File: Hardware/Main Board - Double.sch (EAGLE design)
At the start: 77 parts, among them J1 MICROMOD-2222-C, J10 MICRO-SD-PUSH-PUSH-EXT-PIN, J2 Vertical Qwiic Connector, J4 QWIIC_RIGHT_ANGLE, J5 CORTEX_JTAG_DEBUG_MINIMUM_PTH, J6 MICROMOD_FUNCTION_MAIN, J7 MICROMOD_FUNCTION_MAIN, Q1 3.1A/30V/105mΩ, U1 STG3856QTR, U2 MCP73831, U5 AP7361C-33

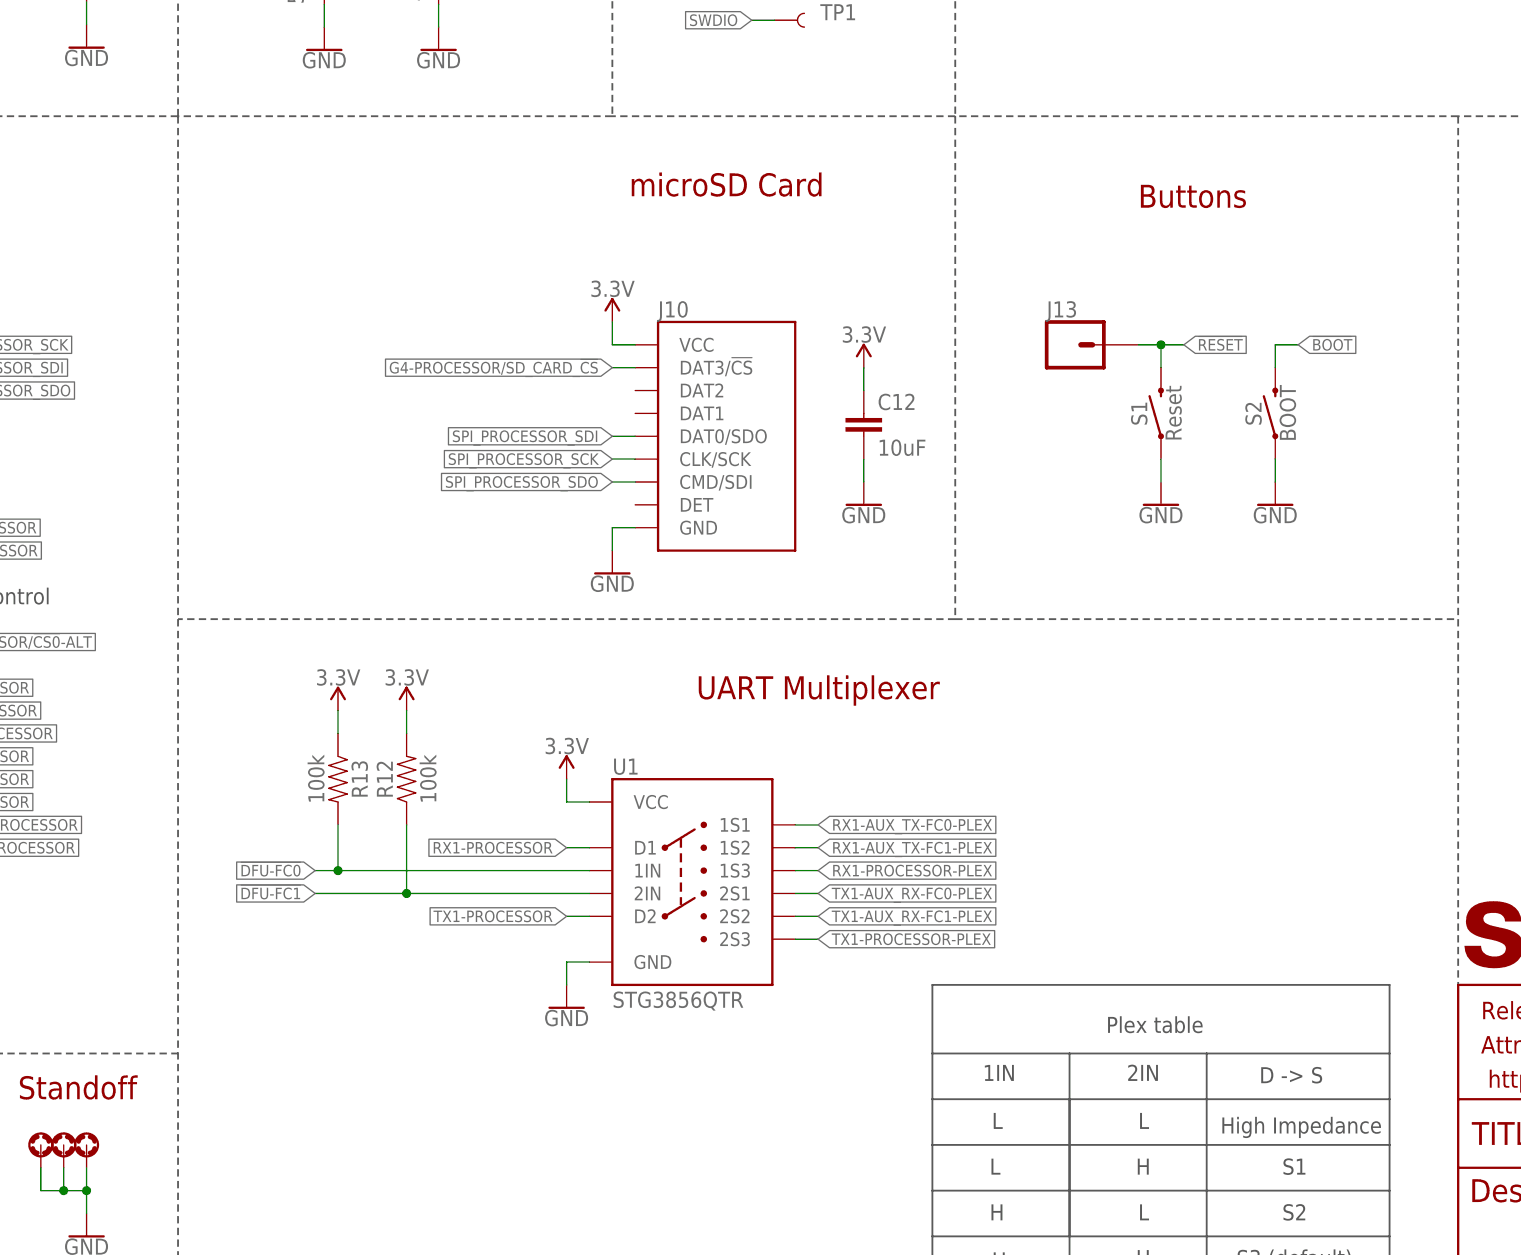
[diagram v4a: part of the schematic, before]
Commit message: Routes airwires
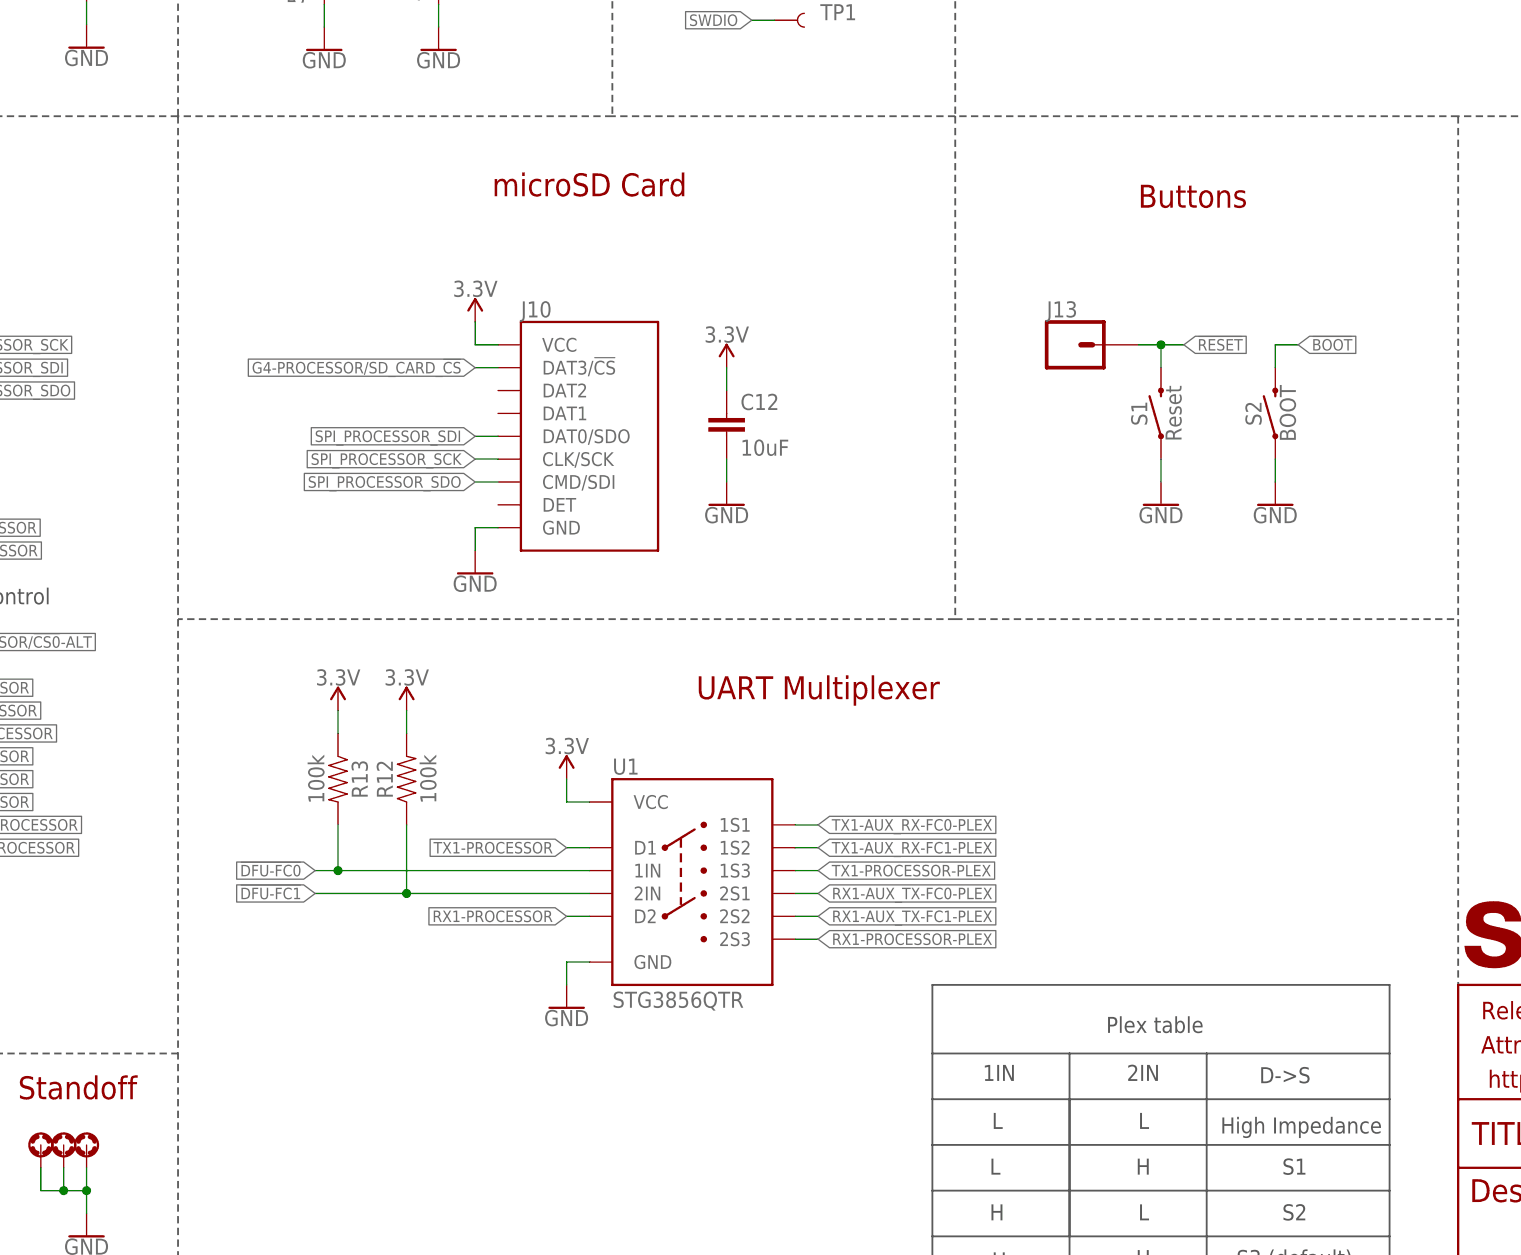
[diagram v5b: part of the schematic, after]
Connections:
- net RX1-AUX_TX-FC0-PLEX: now also U1.2S1; no longer U1.1S1
- net RX1-AUX_TX-FC1-PLEX: now also U1.2S2; no longer U1.1S2
- net RX1-PROCESSOR: now also U1.D2; no longer U1.D1
- net RX1-PROCESSOR-PLEX: now also U1.2S3; no longer U1.1S3
- net TX1-AUX_RX-FC0-PLEX: now also U1.1S1; no longer U1.2S1
- net TX1-AUX_RX-FC1-PLEX: now also U1.1S2; no longer U1.2S2
- net TX1-PROCESSOR: now also U1.D1; no longer U1.D2
- net TX1-PROCESSOR-PLEX: now also U1.1S3; no longer U1.2S3
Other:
- note added: "D->S"
- note removed: "D -> S"
- moved on the sheet: C12, J10

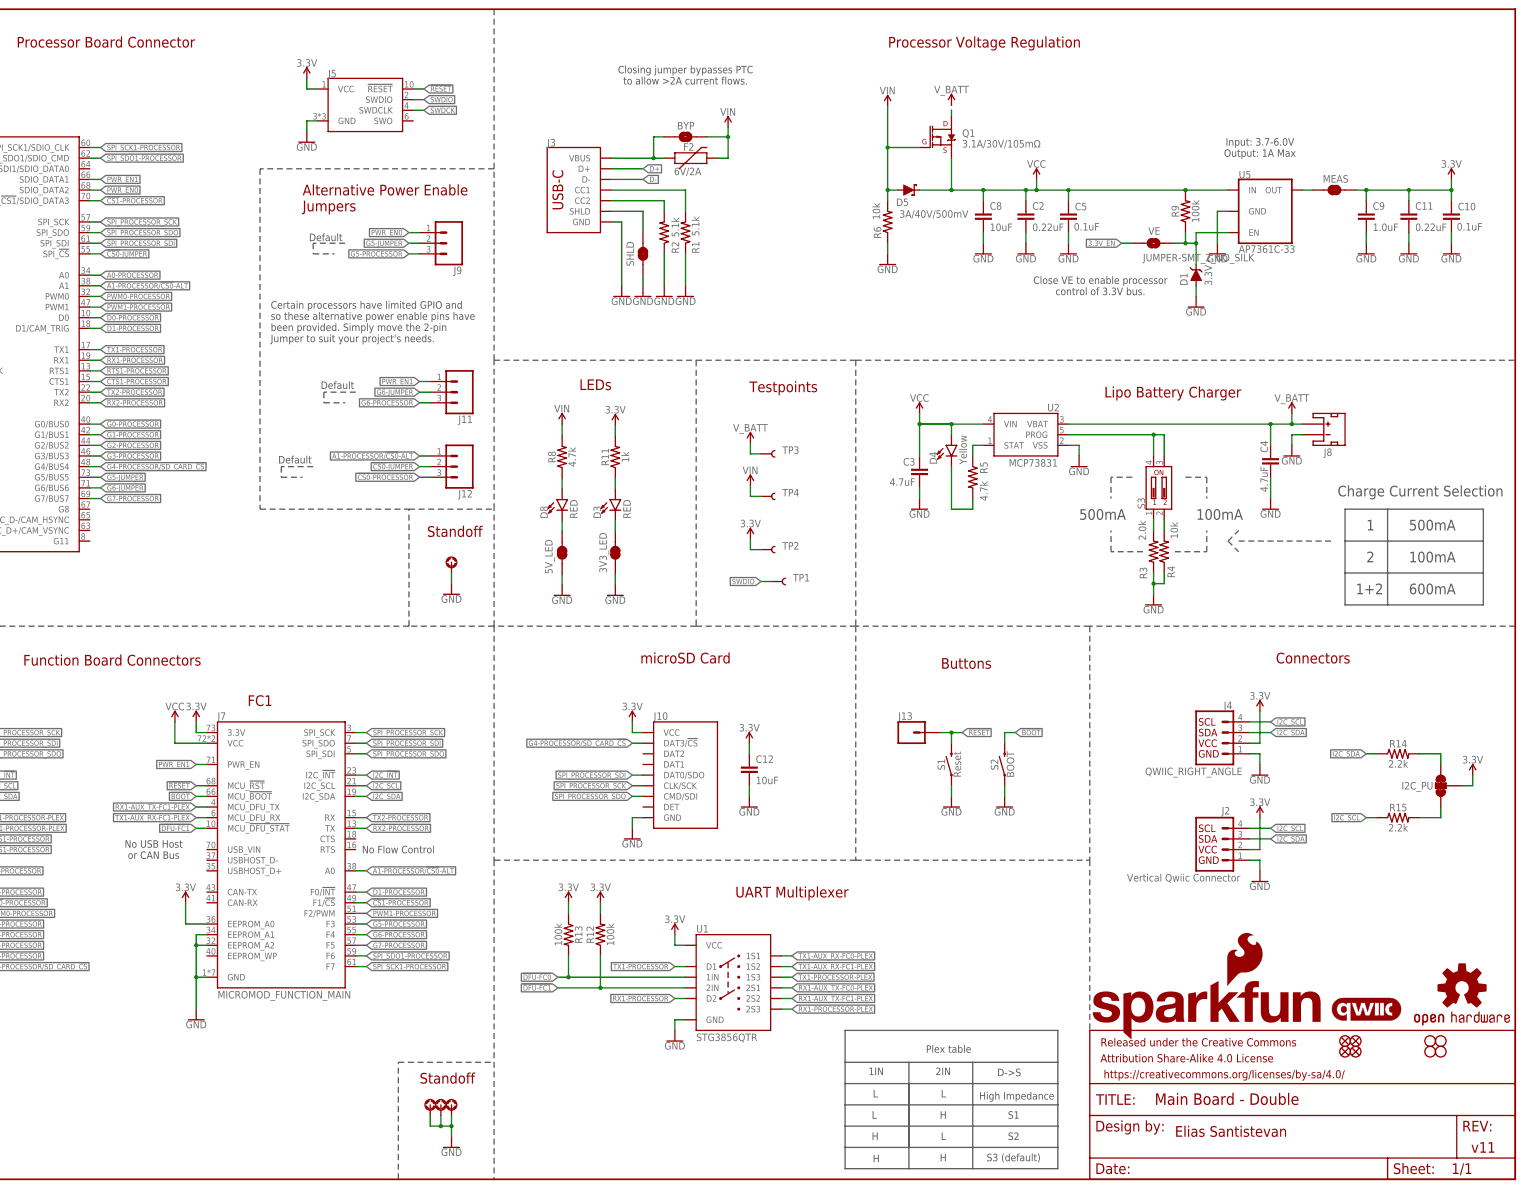
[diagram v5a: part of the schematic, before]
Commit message: Updates design with new dip switch
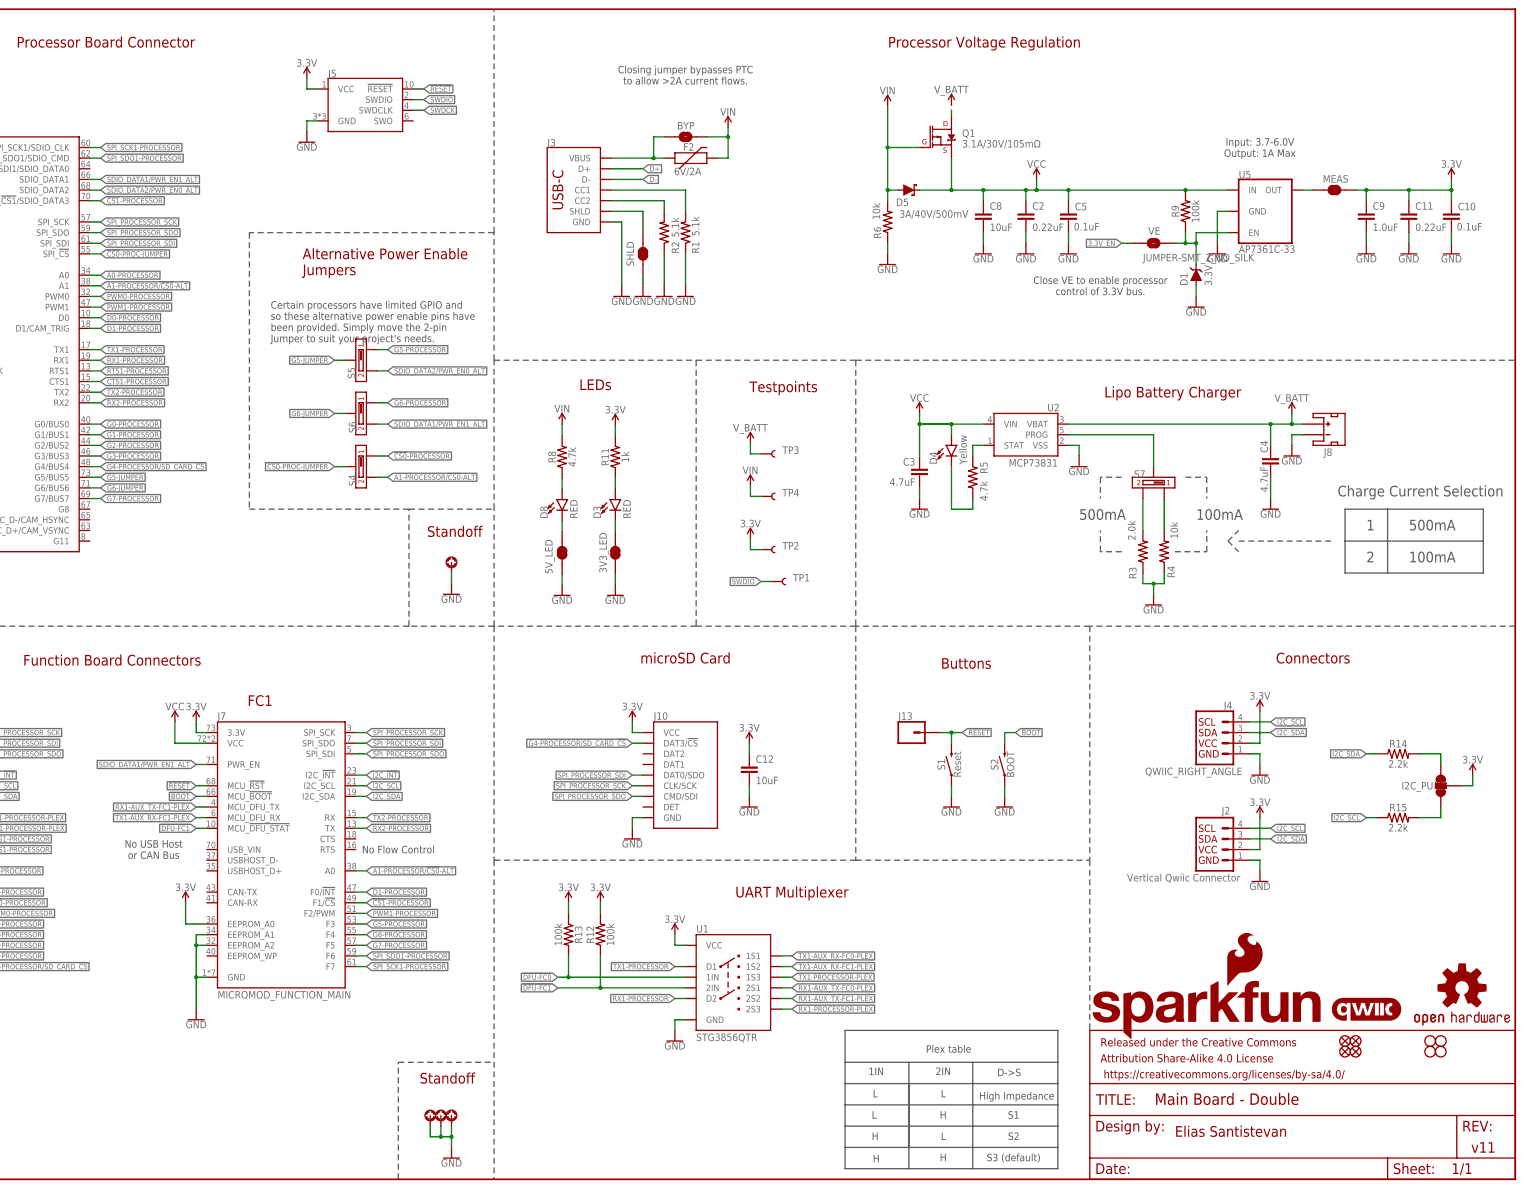
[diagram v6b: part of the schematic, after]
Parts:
- removed J11, J12, J9: (no value), SparkFun-Connectors:CONN_03LOCK
- removed S3: DIP-02-SMD-50MIL, SparkFun-Switches:DIP-02-SMD-50MIL
- added S4, S5, S6, S7: DIPSWITCH-3-PIN, dip_switch:DIPSWITCH-3-PIN
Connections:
- removed net !CS0!-JUMPER: J1.SPI_!CS!, J12.2
- removed net PWR_EN1: J1.SDIO_DATA1, J11.1, J7.PWR_EN
- new net !CS0!-PROC-JUMPER: J1.SPI_!CS!, S4.2
- new net SDIO_DATA1/PWR_EN1_ALT: J1.SDIO_DATA1, J7.PWR_EN, S6.1
- new net SDIO_DATA2/PWR_EN0_ALT: J1.SDIO_DATA2, S5.1
- net !CS0!-PROCESSOR: now also S4.3; no longer J12.3
- net A1-PROCESSOR/!CS0!-ALT: now also S4.1; no longer J12.1
- net G5-JUMPER: now also S5.2; no longer J9.2
- net G5-PROCESSOR: now also S5.3; no longer J9.3
- net G6-JUMPER: now also S6.2; no longer J11.2
- net G6-PROCESSOR: now also S6.3; no longer J11.3
- net N$6: now also S7.2; no longer S3.P$3, S3.P$4
- net N$8: now also S7.1; no longer S3.P$1
- net N$9: now also S7.3; no longer S3.P$2
- net PWR_EN0: no longer J1.SDIO_DATA2, J9.1
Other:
- note removed: "1+2"
- note removed: "600mA"
- note removed: "Default"
- moved on the sheet: R3

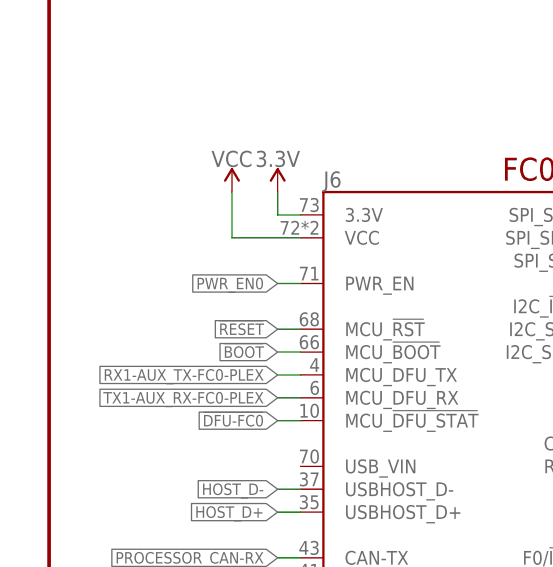
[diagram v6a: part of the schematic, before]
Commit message: Large rework in which many of the traces were routed to leave more space between them.
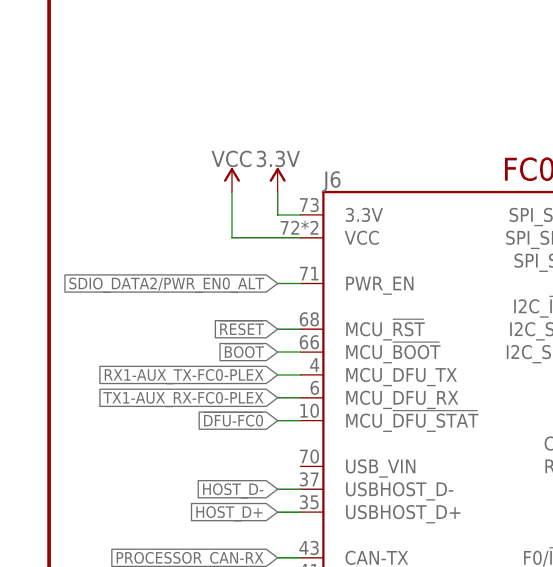
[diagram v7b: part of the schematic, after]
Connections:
- removed net PWR_EN0: J6.PWR_EN
- net SDIO_DATA2/PWR_EN0_ALT: now also J6.PWR_EN
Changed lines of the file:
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@@
-</segment>
-</net>
-<net name="PWR_EN0" class="0">
-<segment>
-<wire x1="27.94" y1="99.06" x2="25.4" y2="99.06" width="0.1524" layer="91"/>
-<label x="25.4" y="99.06" size="1.27" layer="95" font="vector" rot="R180" xref="yes"/>
-<pinref part="J6" gate="J1" pin="PWR_EN"/>
 </segment>
 </net>
@@
 <label x="93.98" y="236.22" size="1.27" layer="95" font="vector" xref="yes"/>
 </segment>
-</net>
+<segment>
+<wire x1="27.94" y1="99.06" x2="25.4" y2="99.06" width="0.1524" layer="91"/>
+<label x="25.4" y="99.06" size="1.27" layer="95" font="vector" rot="R180" xref="yes"/>
+<pinref part="J6" gate="J1" pin="PWR_EN"/>
+</segment>
+</net>

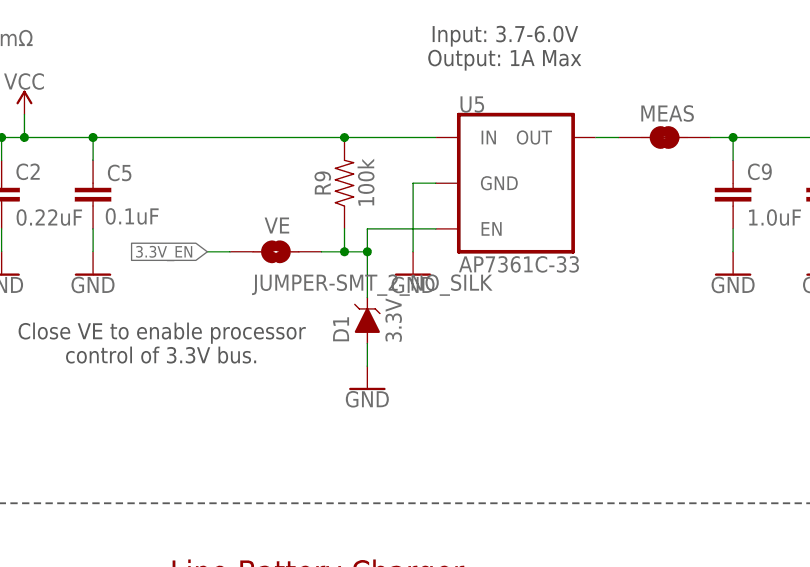
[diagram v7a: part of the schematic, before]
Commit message: Fixes some vias, deletes value of jumper
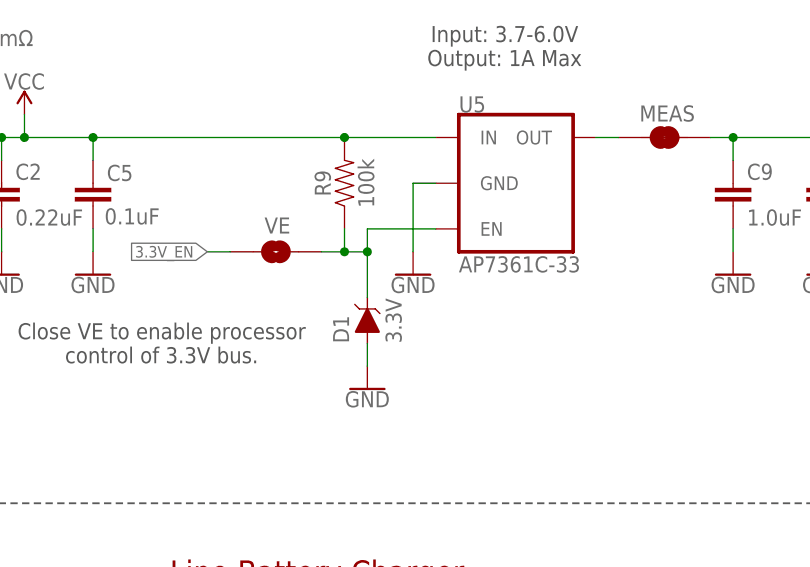
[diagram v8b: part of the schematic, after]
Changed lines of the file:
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@@
 <instance part="VE" gate="G$1" x="345.44" y="223.52" smashed="yes">
 <attribute name="NAME" x="344.17" y="225.552" size="1.778" layer="95" font="vector"/>
-<attribute name="VALUE" x="342.9" y="220.98" size="1.778" layer="96" font="vector" align="top-left"/>
 </instance>
 <instance part="3V3_LED" gate="G$1" x="216.916" y="149.606" smashed="yes" rot="R90">
